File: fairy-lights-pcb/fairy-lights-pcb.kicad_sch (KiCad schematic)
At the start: 16 parts, among them J1 Power_Jack, J2 Conn_LED_Strand, J3 Conn_LED_Strand, J4 Conn_Misc, J5 Conn_02x04_Top_Bottom, SW1 SW_PWR, SW2 SW_User, U1 WeMos_D1_mini, U2 TXS0108EPW

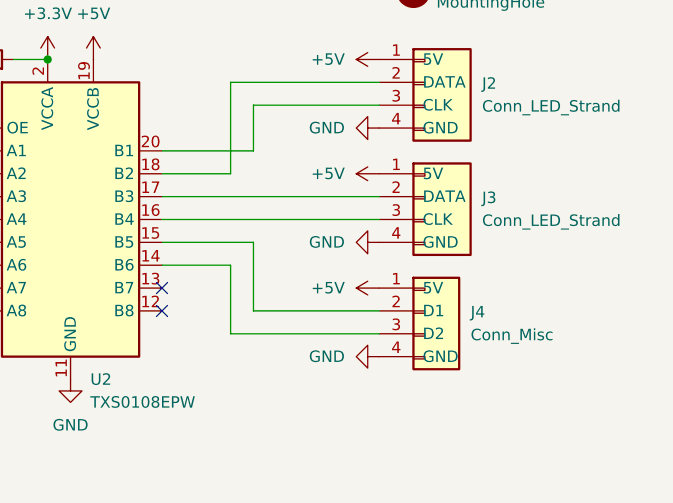
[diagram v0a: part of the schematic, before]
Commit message: Update pins and labels
- All MCU pin silkscreen labels should now be correct.
- The board title is updated to say "r(evision)" instead of "v(ersion)".
- The middle pins of J3 and J4 are swapped for totally valid reasons
  (viz. schematic symmetry).
- J4 is turned into a LED strand connector (such that its pin labels
  match the I2C functions of the corresponding MCU pins).
- Traces are rerouted to account for the schematic changes and to reduce
  ugly spots.
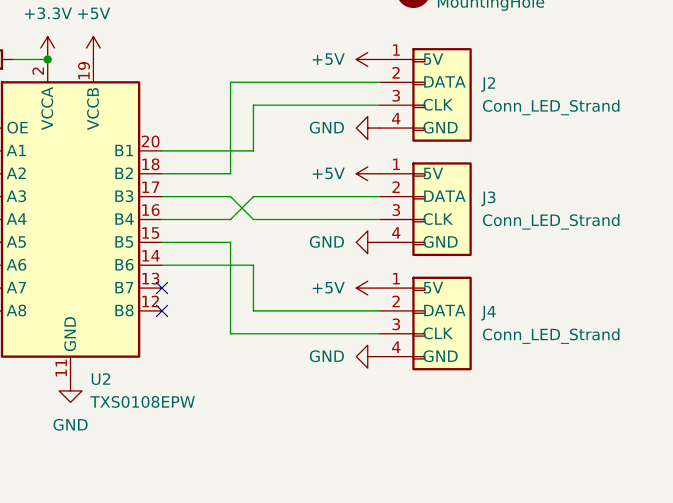
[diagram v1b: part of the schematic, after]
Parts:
- J4: value Conn_Misc -> Conn_LED_Strand; symbol CustomSymbols:Conn_Misc -> CustomSymbols:Conn_LED_Strand
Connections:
- net at J3.2 (DATA): now also U2.16 (B4); no longer U2.17 (B3)
- net at J3.3 (CLK): now also U2.17 (B3); no longer U2.16 (B4)
- net at J4.2 (DATA): now also U2.14 (B6); no longer U2.15 (B5)
- net at J4.3 (CLK): now also U2.15 (B5); no longer U2.14 (B6)
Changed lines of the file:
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@@
+	(wire
+		(pts
+			(xy 175.26 81.28) (xy 185.42 81.28)
+		)
+		(stroke
+			(width 0)
+			(type default)
+		)
+	)
 	(wire
 		(pts
@@
 	(wire
 		(pts
+			(xy 182.88 78.74) (xy 182.88 88.9)
+		)
+		(stroke
+			(width 0)
+			(type default)
+		)
+	)
+	(wire
+		(pts
 			(xy 185.42 68.58) (xy 185.42 63.5)
 		)
@@
 	(wire
 		(pts
-			(xy 175.26 78.74) (xy 185.42 78.74)
+			(xy 175.26 78.74) (xy 182.88 78.74)
 		)
 		(stroke
@@
 	(wire
 		(pts
-			(xy 185.42 78.74) (xy 185.42 86.36)
-		)
-		(stroke
-			(width 0)
-			(type default)
-		)
-	)
-	(wire
-		(pts
 			(xy 182.88 60.96) (xy 199.39 60.96)
 		)
@@
 	(wire
 		(pts
+			(xy 182.88 73.66) (xy 185.42 76.2)
+		)
+		(stroke
+			(width 0)
+			(type default)
+		)
+	)
+	(wire
+		(pts
 			(xy 175.26 68.58) (xy 185.42 68.58)
 		)
@@
 	(wire
 		(pts
-			(xy 175.26 76.2) (xy 199.39 76.2)
+			(xy 175.26 76.2) (xy 182.88 76.2)
 		)
 		(stroke
@@
 	(wire
 		(pts
+			(xy 182.88 76.2) (xy 185.42 73.66)
+		)
+		(stroke
+			(width 0)
+			(type default)
+		)
+	)
+	(wire
+		(pts
 			(xy 124.46 78.74) (xy 142.24 78.74)
 		)
@@
 	(wire
 		(pts
+			(xy 185.42 81.28) (xy 185.42 86.36)
+		)
+		(stroke
+			(width 0)
+			(type default)
+		)
+	)
+	(wire
+		(pts
 			(xy 152.4 78.74) (xy 154.94 78.74)
 		)
@@
 	(wire
 		(pts
-			(xy 175.26 73.66) (xy 199.39 73.66)
+			(xy 185.42 73.66) (xy 199.39 73.66)
+		)
+		(stroke
+			(width 0)
+			(type default)
+		)
+	)
+	(wire
+		(pts
+			(xy 175.26 73.66) (xy 182.88 73.66)
 		)
 		(stroke
@@
 	(wire
 		(pts
+			(xy 185.42 86.36) (xy 199.39 86.36)
+		)
+		(stroke
+			(width 0)
+			(type default)
+		)
+	)
+	(wire
+		(pts
 			(xy 139.7 83.82) (xy 152.4 71.12)
 		)
@@
 	(wire
 		(pts
-			(xy 182.88 81.28) (xy 182.88 88.9)
-		)
-		(stroke
-			(width 0)
-			(type default)
-		)
-	)
-	(wire
-		(pts
 			(xy 124.46 68.58) (xy 142.24 68.58)
 		)
@@
 	(wire
 		(pts
-			(xy 185.42 86.36) (xy 199.39 86.36)
-		)
-		(stroke
-			(width 0)
-			(type default)
-		)
-	)
-	(wire
-		(pts
-			(xy 175.26 81.28) (xy 182.88 81.28)
+			(xy 182.88 88.9) (xy 199.39 88.9)
 		)
 		(stroke
@@
 	(wire
 		(pts
-			(xy 182.88 88.9) (xy 199.39 88.9)
+			(xy 185.42 76.2) (xy 199.39 76.2)
 		)
 		(stroke
@@
 	)
 	(symbol
-		(lib_id "CustomSymbols:Conn_Misc")
+		(lib_id "CustomSymbols:Conn_LED_Strand")
 		(at 203.2 87.63 0)
 		(unit 1)
@@
 		(fields_autoplaced yes)
 		(property "Reference" "J4"
-			(at 209.55 86.4869 0)
-			(effects
-				(font
-					(size 1.27 1.27)
-				)
-				(justify left)
-			)
-		)
-		(property "Value" "Conn_Misc"
-			(at 209.55 89.0269 0)
+			(at 210.82 86.4869 0)
+			(effects
+				(font
+					(size 1.27 1.27)
+				)
+				(justify left)
+			)
+		)
+		(property "Value" "Conn_LED_Strand"
+			(at 210.82 89.0269 0)
 			(effects
 				(font
@@
 			)
 		)
-		(property "Description" "Miscellaneous connector"
+		(property "Description" "LED strand connector"
 			(at 204.47 86.36 0)
 			(effects

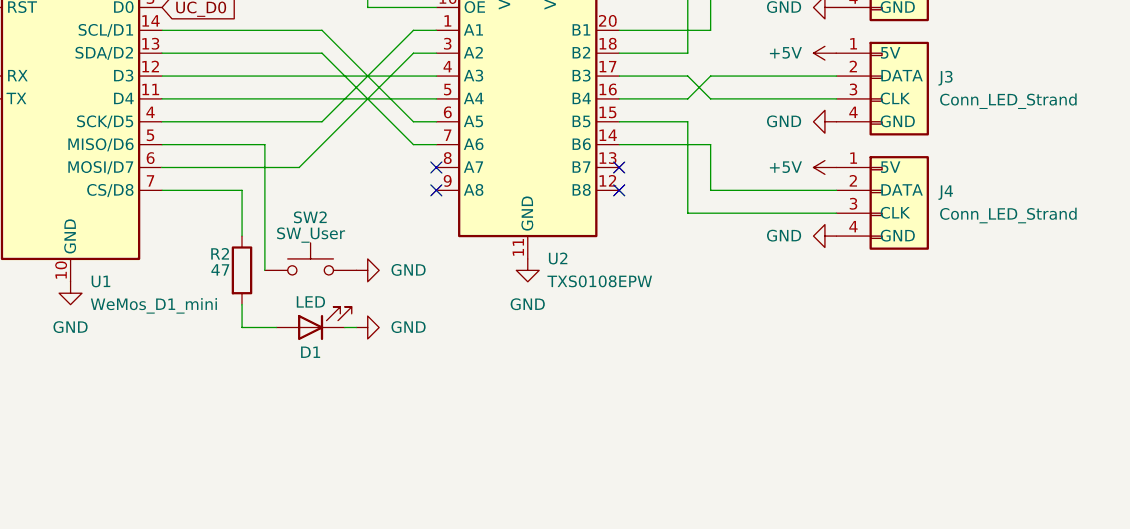
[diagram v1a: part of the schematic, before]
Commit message: Use different status LED
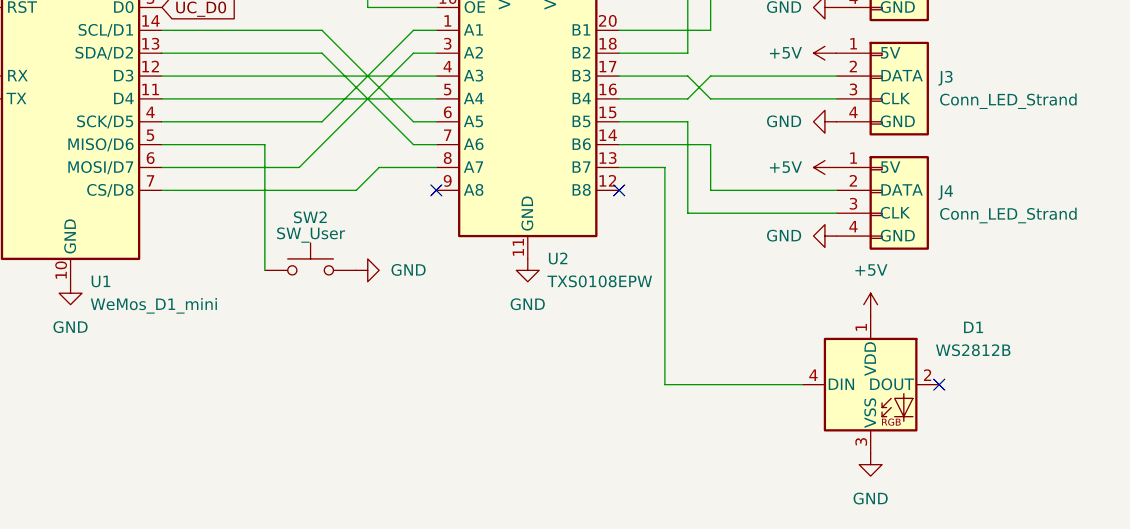
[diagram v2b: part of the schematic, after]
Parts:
- removed D1: LED, LED_THT:LED_D3.0mm, symbol Device:LED
- removed R2: 47, Resistor_THT:R_Axial_DIN0204_L3.6mm_D1.6mm_P7.62mm_Horizontal, symbol Device:R
- added D1: WS2812B, LED_SMD:LED_WS2812B_PLCC4_5.0x5.0mm_P3.2mm, symbol LED:WS2812B
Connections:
- net +5V: now also D1.1 (VDD)
- net GND: now also D1.3 (VSS)
- net at U1.7 (CS/D8): now also U2.8 (A7)
- net at U2.13 (B7): now also D1.4 (DIN)
- no-connect marks 4 -> 3

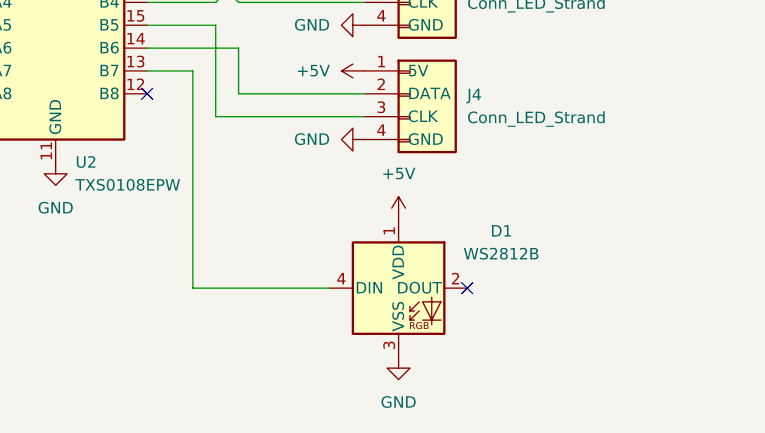
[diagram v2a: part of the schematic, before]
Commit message: Moar LEDs
We're also considering yeeting or replacing the level shifter. Until we
decide on what the replacement will be, I'll leave the current one in,
with the understanding that one could substitute a pin-compatible and
working replacement.
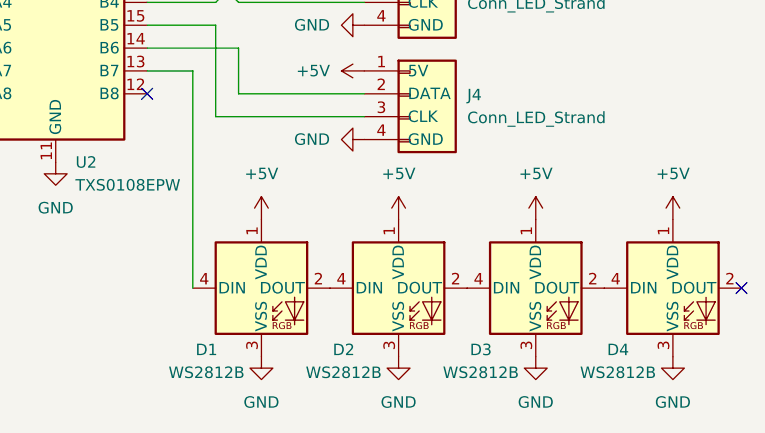
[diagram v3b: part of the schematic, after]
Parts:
- added D2, D3, D4: WS2812B, LED_SMD:LED_WS2812B_PLCC4_5.0x5.0mm_P3.2mm, symbol LED:WS2812B
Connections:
- net +5V: now also D2.1 (VDD), D3.1 (VDD), D4.1 (VDD)
- net GND: now also D2.3 (VSS), D3.3 (VSS), D4.3 (VSS)
- net at D1.2 (DOUT): now also D2.4 (DIN)
- new net: D3.2 (DOUT), D4.4 (DIN)
- new net: D2.2 (DOUT), D3.4 (DIN)
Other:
- moved on the sheet: D1

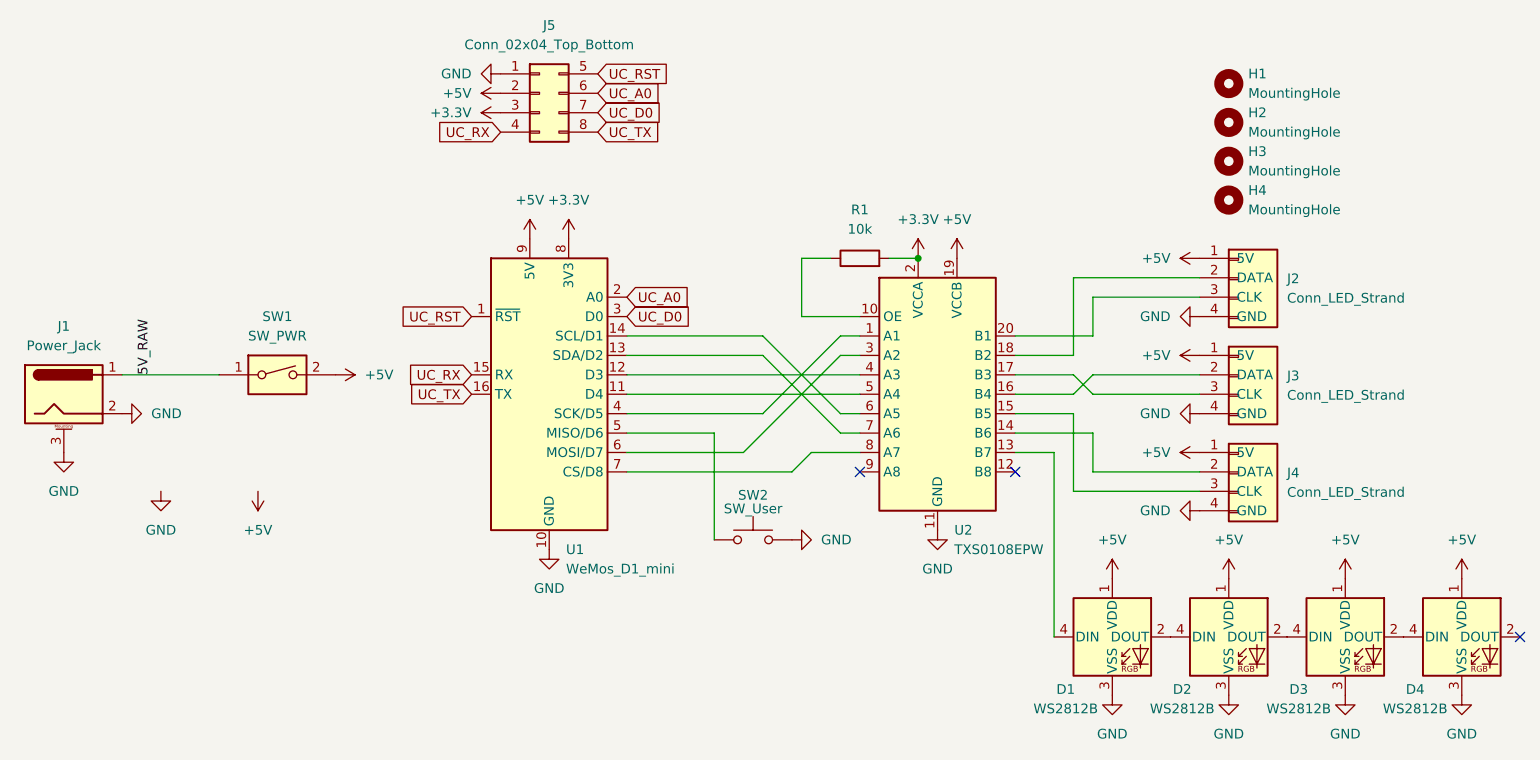
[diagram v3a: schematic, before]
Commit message: Yeet level shifter; update interfaces
- The level shifter we planned to use seems not to work on a breadboard.
- Driving the LED controllers with 3.3V signals directly instead seems
  to work (although it is out-of-spec or barely at the boundary of what
  is in-spec).
- LED strands are now attached via screw terminals. (Of course, one can
  choose not to populate them and solder wires directly to the pads
  instead.)
- The size of one of the terminals is reduced to three signals, to
  accomodate WS2812 LED strands.
- The thus-free GPIO pin is repurposed to be another switch.
- Changed user switches to tactile vertical push buttons.
- Updated parts list in README.
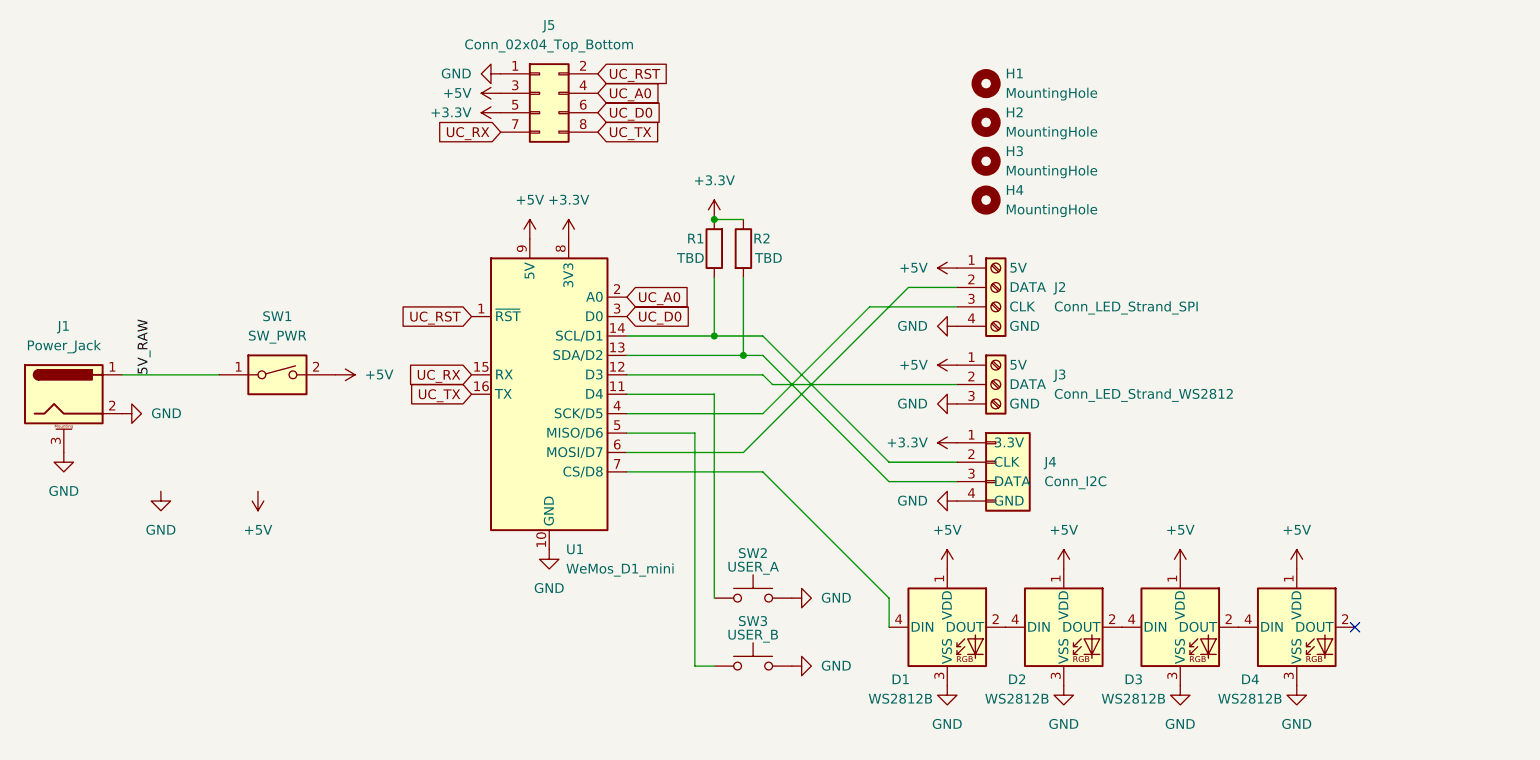
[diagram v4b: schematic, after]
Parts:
- removed U2: TXS0108EPW, CustomLibrary:Texas_TXS0108E_Level_Shifter_Module, symbol CustomSymbols:TXS0108EPW
- added R2: TBD, Resistor_THT:R_Axial_DIN0204_L3.6mm_D1.6mm_P7.62mm_Horizontal, symbol Device:R
- added SW3: USER_B, Button_Switch_THT:SW_Tactile_SPST_Angled_PTS645Vx31-2LFS, symbol Switch:SW_Push
- J2: value Conn_LED_Strand -> Conn_LED_Strand_SPI; footprint Connector_PinHeader_2.54mm:PinHeader_1x04_P2.54mm_Vertical -> TerminalBlock_Phoenix:TerminalBlock_Phoenix_MKDS-1,5-4_1x04_P5.00mm_Horizontal; symbol CustomSymbols:Conn_LED_Strand -> CustomSymbols:Conn_LED_Strand_SPI
- J3: value Conn_LED_Strand -> Conn_LED_Strand_WS2812; footprint Connector_PinHeader_2.54mm:PinHeader_1x04_P2.54mm_Vertical -> TerminalBlock_Phoenix:TerminalBlock_Phoenix_MKDS-1,5-3_1x03_P5.00mm_Horizontal; symbol CustomSymbols:Conn_LED_Strand -> CustomSymbols:Conn_LED_Strand_WS2812
- J4: value Conn_LED_Strand -> Conn_I2C; symbol CustomSymbols:Conn_LED_Strand -> CustomSymbols:Conn_I2C
- J5: symbol Connector_Generic:Conn_02x04_Top_Bottom -> Connector_Generic:Conn_02x04_Odd_Even
- R1: value 10k -> TBD
- SW2: value SW_User -> USER_A; footprint Connector_PinHeader_2.54mm:PinHeader_1x02_P2.54mm_Vertical -> Button_Switch_THT:SW_Tactile_SPST_Angled_PTS645Vx31-2LFS
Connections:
- net +3.3V: now also J4.1 (3.3V), J5.5 (Pin_5), R2.1; no longer J5.3 (Pin_3)
- net +5V: now also J5.3 (Pin_3); no longer J4.1 (5V), J5.2 (Pin_2)
- net GND: now also J3.3 (GND), SW3.2; no longer J3.4 (GND)
- net UC_A0: now also J5.4 (Pin_4); no longer J5.6 (Pin_6)
- net UC_D0: now also J5.6 (Pin_6); no longer J5.7 (Pin_7)
- net UC_RST: now also J5.2 (Pin_2); no longer J5.5 (Pin_5)
- net UC_RX: now also J5.7 (Pin_7); no longer J5.4 (Pin_4)
- net at U1.5 (MISO/D6): now also SW3.1; no longer SW2.1
- net at J3.2 (DATA): now also U1.12 (D3)
- net at J2.2 (DATA): now also U1.6 (MOSI/D7)
- net at J2.3 (CLK): now also U1.4 (SCK/D5)
- net at J4.2 (CLK): now also R1.1, U1.14 (SCL/D1)
- net at J4.3 (DATA): now also U1.13 (SDA/D2), R2.2
- net at D1.4 (DIN): now also U1.7 (CS/D8)
- net at U1.11 (D4): now also SW2.1
- no-connect marks 3 -> 1
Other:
- moved on the sheet: D1, D2, D3, D4, H1, H2, H3, H4, J4, SW2
